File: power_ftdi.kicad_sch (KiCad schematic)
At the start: 0 parts

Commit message: develop: Started adding more stuff. Started symbol for FPGA.
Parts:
- added J3: USB_C_Receptacle_USB2.0_14P, symbol Connector:USB_C_Receptacle_USB2.0_14P
- added U3: FT4232H, symbol Interface_USB:FT4232H
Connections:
- new net: J3.A1 (GND), J3.A12 (GND), J3.B1 (GND), J3.B12 (GND)
- new net: J3.A4 (VBUS), J3.A9 (VBUS), J3.B4 (VBUS), J3.B9 (VBUS)

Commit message: develop: Did some stuff. Not sure what I am doing :).
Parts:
- removed J3: USB_C_Receptacle_USB2.0_14P, symbol Connector:USB_C_Receptacle_USB2.0_14P
- added R4, R5: 100k, symbol Device:R
- added SW1: CK_KMS2xxGP, Button_Switch_SMD:SW_SPST_CK_KMS2xxGP, symbol Switch:CK_KMS2xxGP
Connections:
- net at U3.14 (~{RESET}): now also R5.2, SW1.2
- net FTDI_DM: now reaches U3.7 (DM)
- net FTDI_DP: now reaches U3.8 (DP)
- new net: R4.1, SW1.SH (B)
- new net 3V3: R5.1
- new net GND: R4.2, SW1.1
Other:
- moved on the sheet: U3

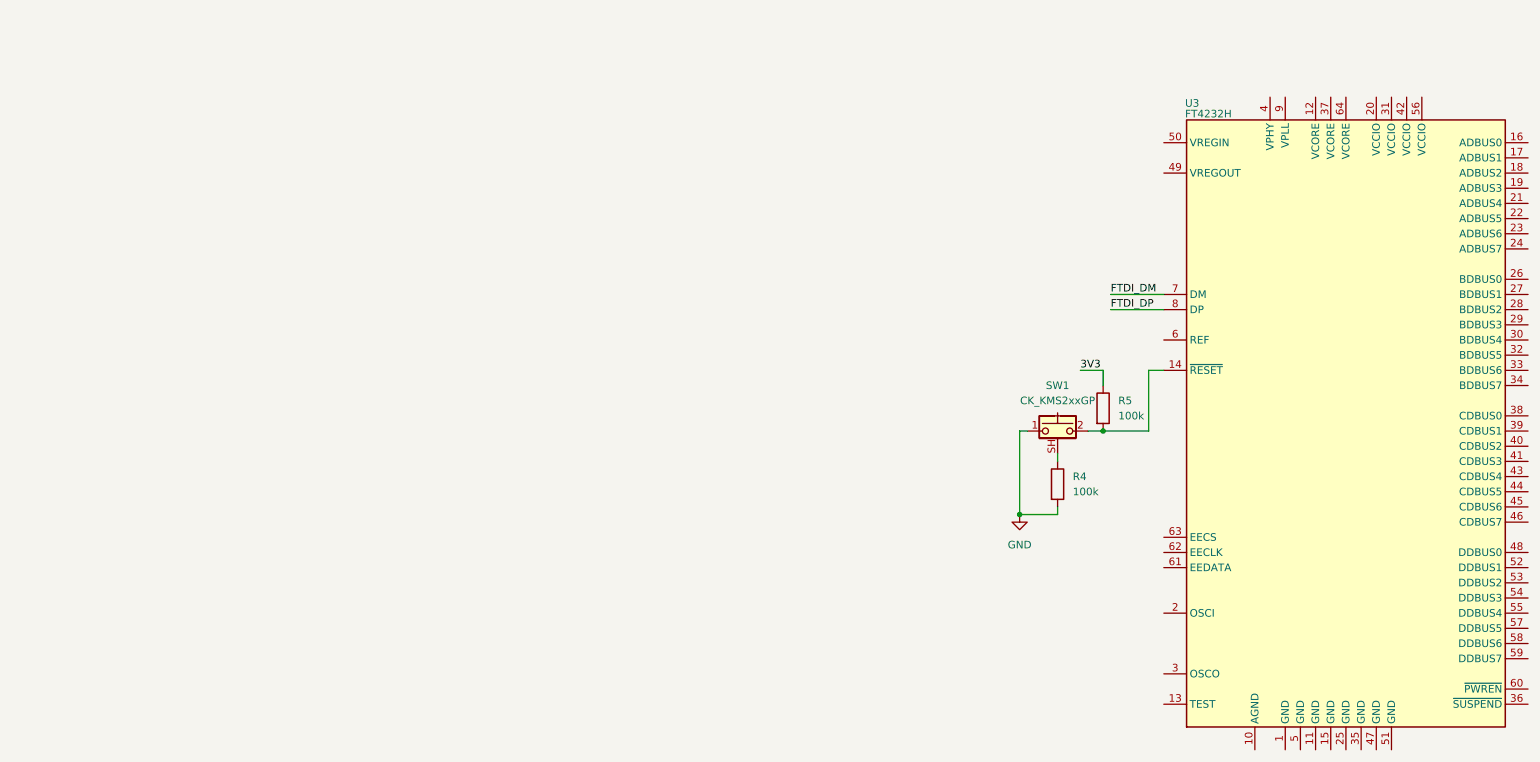
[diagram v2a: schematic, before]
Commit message: develop: Added 1.8/3.3V and 0.95V power regulators.
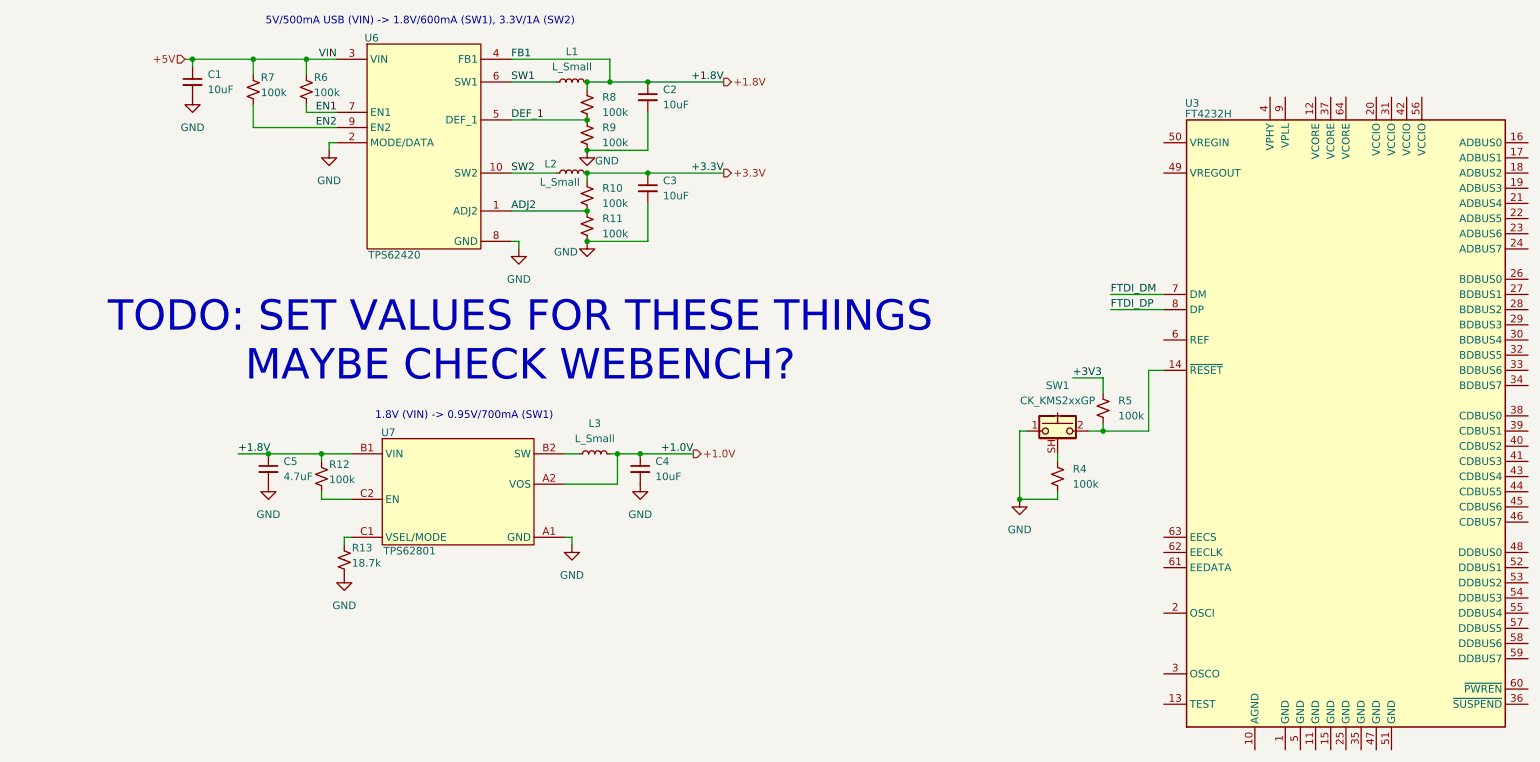
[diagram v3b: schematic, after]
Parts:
- added C1, C2, C3, C4: 10uF, Capacitor_SMD:C_01005_0402Metric, symbol Device:C_Small
- added C5: 4.7uF, Capacitor_SMD:C_01005_0402Metric, symbol Device:C_Small
- added L1, L2, L3: L_Small, symbol Device:L_Small
- added R10, R11, R12, R6, R7, R8, R9: 100k, symbol Device:R_Small_US
- added R13: 18.7k, symbol Device:R_Small_US
- added U6: TPS62420, Package_SON:Texas_S-PVSON-N10, symbol duality:TPS62420
- added U7: TPS62801, duality:BGA-6_2x3_0.734x1.084mm, symbol duality:TPS62801
- R4, R5: symbol Device:R -> Device:R_Small_US
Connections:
- net GND: now also C1.2, C2.2, C3.2, C4.2, C5.2, R11.2, R13.2, R9.2, U6.2 (MODE/DATA), U6.8 (GND), U7.A1 (GND)
- net 3V3 renamed +3V3
- new net: L3.1, U7.B2 (SW)
- new net: R13.1, U7.C1 (VSEL/MODE)
- new net: R12.2, U7.C2 (EN)
- new net +1.0V: C4.1, L3.2, U7.A2 (VOS)
- new net +1.8V: C2.1, C5.1, L1.2, R12.1, R8.1, U6.4 (FB1), U7.B1 (VIN)
- new net +3.3V: C3.1, L2.2, R10.1
- new net +5V: C1.1, R6.1, R7.1, U6.3 (VIN)
- new net ADJ2: R10.2, R11.1, U6.1 (ADJ2)
- new net DEF_1: R8.2, R9.1, U6.5 (DEF_1)
- new net EN1: R6.2, U6.7 (EN1)
- new net EN2: R7.2, U6.9 (EN2)
- new net SW1: L1.1, U6.6 (SW1)
- new net SW2: L2.1, U6.10 (SW2)
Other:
- note added: "1.8V (VIN) -> 0.95V/700mA (SW1)"
- note added: "5V/500mA USB (VIN) -> 1.8V/600mA (SW1), 3.3V/1A (SW2)"
- note added: "TODO: SET VALUES FOR THESE THINGS MAYBE CHECK WEBENCH?"
